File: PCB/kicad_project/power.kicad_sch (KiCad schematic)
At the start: 16 parts, among them U2 TPS74801DRC, U3 TPS82130, U4 REF3020

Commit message: TPS82130 fb
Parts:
- R9: value 100kΩ -> 309kΩ
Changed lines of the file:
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@@
 			)
 		)
-		(property "Value" "100kΩ"
+		(property "Value" "309kΩ"
 			(at 79.502 90.17 90)
 			(effects

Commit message: MCU部分扇出，SDRAM走线ing
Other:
- moved on the sheet: C43, C44, C45, C46, R10, R9, U3, U4

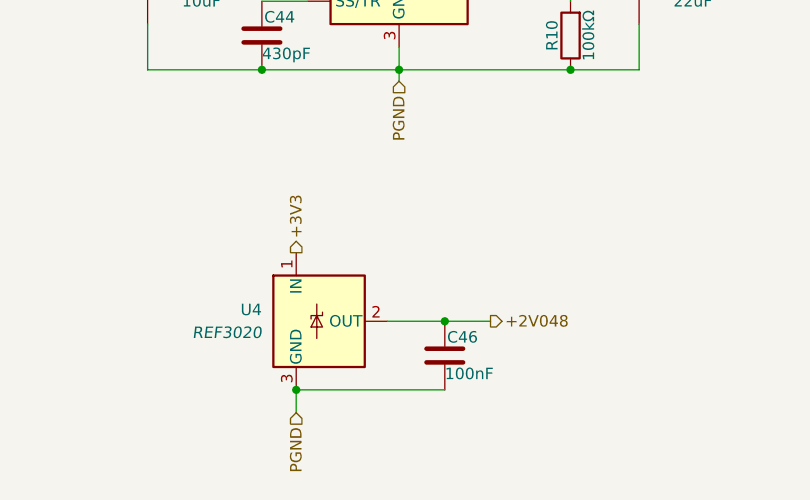
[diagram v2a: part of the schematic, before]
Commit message: 铺铜，增加BTB
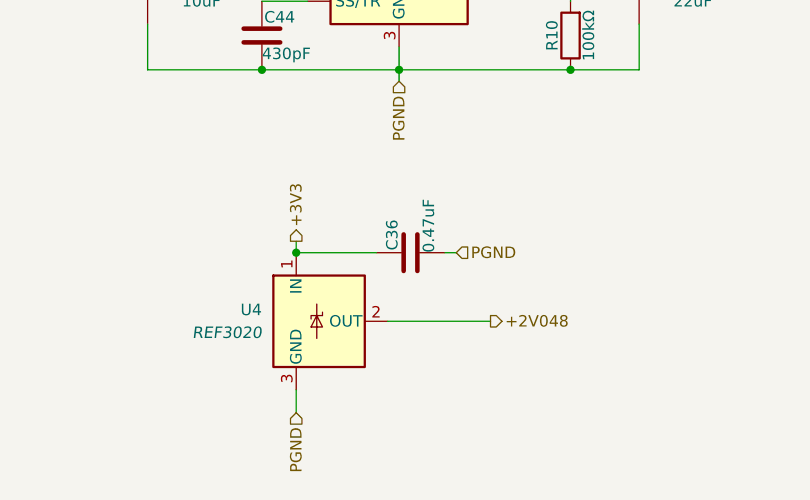
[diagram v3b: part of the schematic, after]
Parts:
- removed C46: 100nF, Capacitor_SMD:C_0402_1005Metric, symbol Device:C
- added C36: 0.47uF, Capacitor_SMD:C_0402_1005Metric, symbol Device:C
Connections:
- net +3V3: now also C36.1
- net PGND: now also C36.2
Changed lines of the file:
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@@
+	)
+	(junction
+		(at 102.87 114.3)
+		(diameter 0)
+		(color 0 0 0 0)
 	)
 	(junction
@@
 	)
 	(junction
-		(at 119.38 121.92)
-		(diameter 0)
-		(color 0 0 0 0)
-	)
-	(junction
 		(at 133.35 76.2)
 		(diameter 0)
@@
 	)
 	(junction
-		(at 102.87 129.54)
-		(diameter 0)
-		(color 0 0 0 0)
-	)
-	(junction
 		(at 147.32 50.8)
 		(diameter 0)
@@
 	(wire
 		(pts
-			(xy 113.03 121.92) (xy 119.38 121.92)
+			(xy 113.03 121.92) (xy 124.46 121.92)
 		)
 		(stroke
@@
 	(wire
 		(pts
-			(xy 102.87 129.54) (xy 119.38 129.54)
-		)
-		(stroke
-			(width 0)
-			(type default)
-		)
-	)
-	(wire
-		(pts
 			(xy 78.74 41.91) (xy 83.82 41.91)
 		)
@@
 	(wire
 		(pts
+			(xy 120.65 114.3) (xy 119.38 114.3)
+		)
+		(stroke
+			(width 0)
+			(type default)
+		)
+	)
+	(wire
+		(pts
 			(xy 147.32 50.8) (xy 147.32 49.53)
 		)
@@
 	(wire
 		(pts
+			(xy 102.87 113.03) (xy 102.87 114.3)
+		)
+		(stroke
+			(width 0)
+			(type default)
+		)
+	)
+	(wire
+		(pts
 			(xy 91.44 35.56) (xy 91.44 41.91)
 		)
@@
 	(wire
 		(pts
-			(xy 119.38 121.92) (xy 124.46 121.92)
-		)
-		(stroke
-			(width 0)
-			(type default)
-		)
-	)
-	(wire
-		(pts
 			(xy 99.06 44.45) (xy 99.06 41.91)
 		)
@@
 		(pts
 			(xy 83.82 76.2) (xy 86.36 76.2)
+		)
+		(stroke
+			(width 0)
+			(type default)
+		)
+	)
+	(wire
+		(pts
+			(xy 102.87 114.3) (xy 111.76 114.3)
 		)
 		(stroke
@@
 	(hierarchical_label "PGND"
 		(shape input)
-		(at 147.32 59.69 180)
+		(at 120.65 114.3 0)
 		(fields_autoplaced yes)
 		(effects
@@
 				(size 1.27 1.27)
 			)
+			(justify left)
+		)
+	)
+	(hierarchical_label "PGND"
+		(shape input)
+		(at 147.32 59.69 180)
+		(fields_autoplaced yes)
+		(effects
+			(font
+				(size 1.27 1.27)
+			)
 			(justify right)
 		)
@@
 	(hierarchical_label "+3V3"
 		(shape output)
-		(at 102.87 114.3 90)
+		(at 102.87 113.03 90)
 		(fields_autoplaced yes)
 		(effects
@@
 	)
 	(symbol
+		(lib_id "Device:C")
+		(at 115.57 114.3 90)
+		(unit 1)
+		(exclude_from_sim no)
+		(in_bom yes)
+		(on_board yes)
+		(dnp no)
+		(property "Reference" "C36"
+			(at 113.538 114.046 0)
+			(effects
+				(font
+					(size 1.27 1.27)
+				)
+				(justify left)
+			)
+		)
+		(property "Value" "0.47uF"
+			(at 117.602 114.3 0)
+			(effects
+				(font
+					(size 1.27 1.27)
+				)
+				(justify left)
+			)
+		)
+		(property "Footprint" "Capacitor_SMD:C_0402_1005Metric"
+			(at 119.38 113.3348 0)
+			(effects
+				(font
+					(size 1.27 1.27)
+				)
+				(hide yes)
+			)
+		)
+		(property "Datasheet" "~"
+			(at 115.57 114.3 0)
+			(effects
+				(font
+					(size 1.27 1.27)
+				)
+				(hide yes)
+			)
+		)
+		(property "Description" "Unpolarized capacitor"
+			(at 115.57 114.3 0)
+			(effects
+				(font
+					(size 1.27 1.27)
+				)
+				(hide yes)
+			)
+		)
+		(pin "2"
+		)
+		(pin "1"
+		)
+		(instances
+			(project "h750xb_core"
+				(path "/a69f31b1-c3a2-49f5-a533-af75e45f29ed/e0128536-73a9-45ac-9dac-95fe4f1a4212"
+					(reference "C36")
+					(unit 1)
+				)
+			)
+		)
+	)
+	(symbol
 		(lib_id "Reference_Voltage:REF3020")
 		(at 105.41 121.92 0)
@@
 					(unit 1)
 				)
-			)
-		)
-	)
-	(symbol
-		(lib_id "Device:C")
-		(at 119.38 125.73 0)
-		(unit 1)
-		(exclude_from_sim no)
-		(in_bom yes)
-		(on_board yes)
-		(dnp no)
-		(property "Reference" "C46"
-			(at 119.634 123.698 0)
-			(effects
-				(font
-					(size 1.27 1.27)
-				)
-				(justify left)
-			)
-		)
-		(property "Value" "100nF"
-			(at 119.38 127.762 0)
-			(effects
-				(font
-					(size 1.27 1.27)
-				)
-				(justify left)
-			)
-		)
-		(property "Footprint" "Capacitor_SMD:C_0402_1005Metric"
-			(at 120.3452 129.54 0)
-			(effects
-				(font
-					(size 1.27 1.27)
-				)
-				(hide yes)
-			)
-		)
-		(property "Datasheet" "~"
-			(at 119.38 125.73 0)
-			(effects
-				(font
-					(size 1.27 1.27)
-				)
-				(hide yes)
-			)
-		)
-		(property "Description" "Unpolarized capacitor"
-			(at 119.38 125.73 0)
-			(effects
-				(font
-					(size 1.27 1.27)
-				)
-				(hide yes)
-			)
-		)
-		(pin "2"
-		)
-		(pin "1"
-		)
-		(instances
-			(project "h750xb_core"
-				(path "/a69f31b1-c3a2-49f5-a533-af75e45f29ed/e0128536-73a9-45ac-9dac-95fe4f1a4212"
-					(reference "C46")
-					(unit 1)
-				)
